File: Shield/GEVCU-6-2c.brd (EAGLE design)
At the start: 114.3 x 116.8 mm, 242 parts, among them IC10 ISO1050DW, IC9 ISO1050DW, U1 ATSAM3X8EA-AU, U11 ADE7913, U12 ADE7913, U24 ADE7913, U3 ADUM3221BRZ, U4 ADUM3221BRZ, U5 ADUM3221BRZ, U6 ADUM3221BRZ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

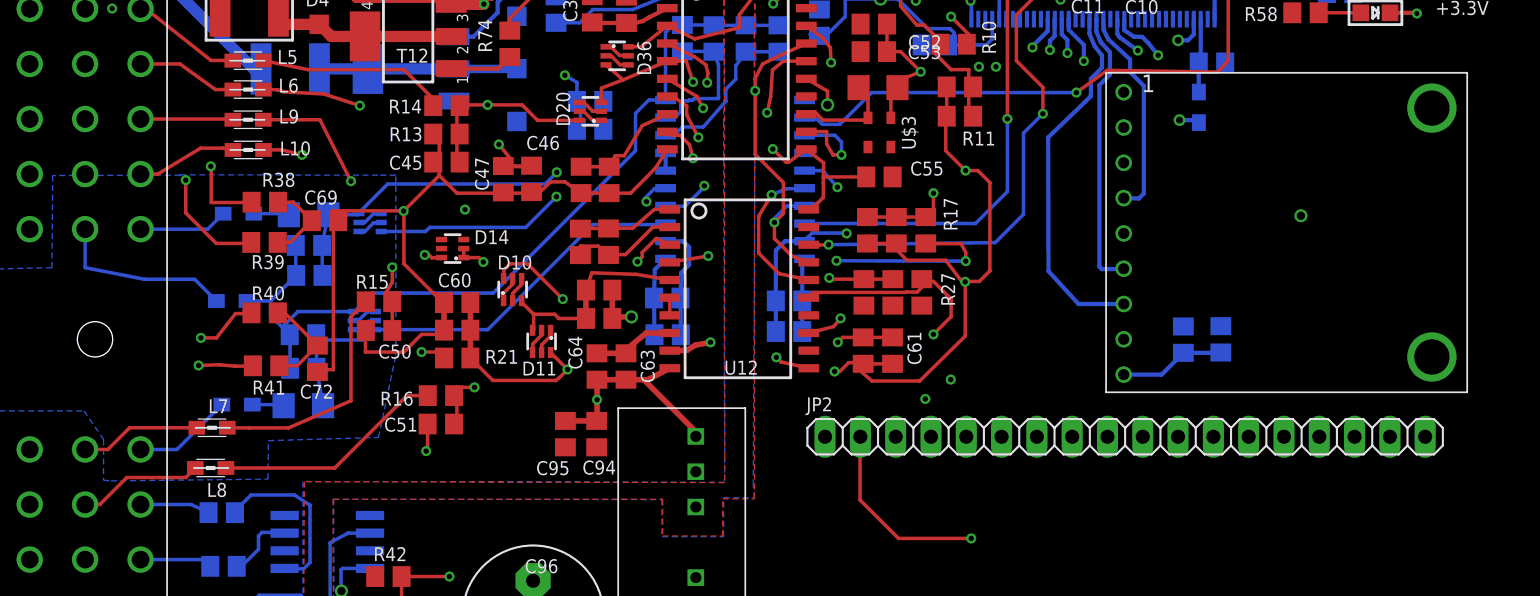
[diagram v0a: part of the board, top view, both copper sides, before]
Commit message: Fixes on GEVCU board files, addition of an Eagle library that contains some of the parts on the GEVCU board.
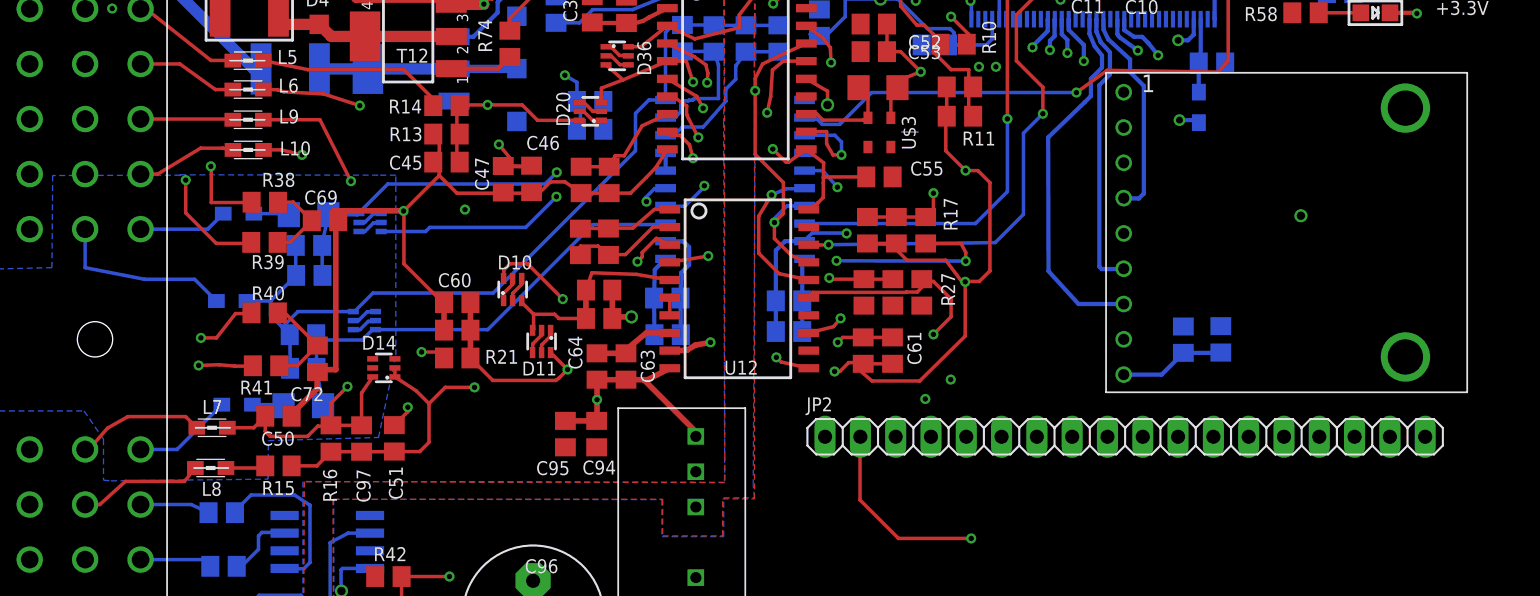
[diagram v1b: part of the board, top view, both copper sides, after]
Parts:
- added C97: 0.1u, rcl:C0805
- R16: value 1k .1% -> 750R .1%
- moved R15 13.9 mm to (22.7, 27.4)
- moved D14 9.91 mm to (30.3, 34.4)
- moved C50 9.51 mm to (22.7, 30.9), turned to 0 degrees
- moved R16 8.49 mm to (26.5, 29.3), turned to 270 degrees
- moved C51 3.49 mm to (31.1, 29.3), turned to 90 degrees
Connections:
- removed net N$20: C50.1, D14.6, R15.1, U11.6
- removed net N$25: L8.1, R16.2
- new net N$7: L8.1, R15.2
- net N$21: now also C97.2, R15.1, R16.2; no longer R16.1
- net N$22: now also C50.1, C97.1, D14.6, R16.1, U11.6; no longer R15.2
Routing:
- net N$20: track 38.6 -> 0.00 mm, vias 3 -> 0
- net N$22: track 17.7 -> 55.9 mm, vias 0 -> 2
- net N$25: track 16.7 -> 0.00 mm
- net N$21: track 44.5 -> 49.9 mm, vias 3 -> 2
- net GND: track 264.4 -> 260.8 mm
- net N$7: track 0.00 -> 2.89 mm
- net SHUNT_L: track 8.68 -> 9.27 mm
